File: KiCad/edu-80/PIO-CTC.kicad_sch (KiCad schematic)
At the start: 2 parts, among them U2 Z84C20, U3 Z8430_CTC

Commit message: Working on removing edu-80-rescue symbol library
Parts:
- U3: symbol edu-80-rescue:Z8430_CTC-Edu-80_Symbol -> Edu-80_Symbols:Z8430_CTC
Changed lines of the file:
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@@
     )
   )
-  (symbol (lib_id "edu-80-rescue:Z8430_CTC-Edu-80_Symbol") (at 161.29 129.54 0) (unit 1)
+  (symbol (lib_id "Edu-80_Symbols:Z8430_CTC") (at 161.29 129.54 0) (unit 1)
     (in_bom yes) (on_board yes) (dnp no)
     (property "Reference" "U3" (at 168.91 110.49 0)

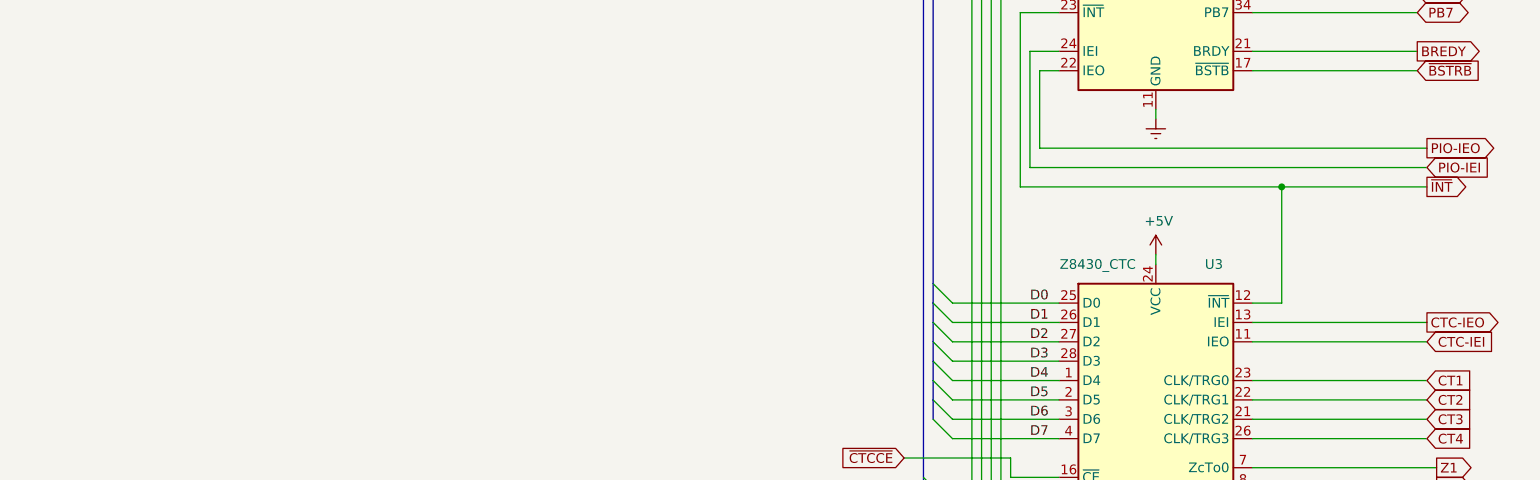
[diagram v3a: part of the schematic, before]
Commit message: Fixed ~IRQ vs. INT for PIO/CTC. Removed old (version 5) schematic files.
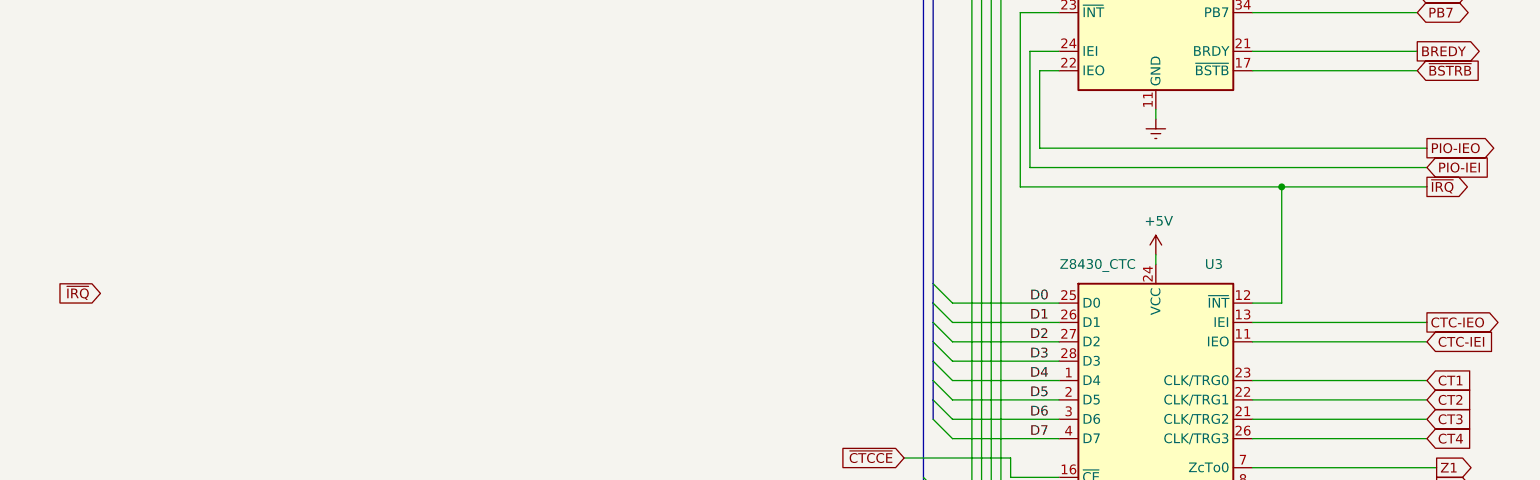
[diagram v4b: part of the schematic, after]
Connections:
- net ~{INT} renamed ~{IRQ}
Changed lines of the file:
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@@
   (title_block
     (title "Edu-80 Z80 Trainer")
-    (date "2023-06-03")
+    (date "2023-06-05")
     (rev "0.1")
     (company "Strangers")
-    (comment 1 "Author: James D. Tucker")
+    (comment 4 "Author: James D. Tucker")
   )
   (junction (at 139.7 67.31) (diameter 0) (color 0 0 0 0)
@@
     )
   )
+  (global_label "~{IRQ}" (shape output) (at 196.85 100.33 0)
+    (effects (font (size 1.27 1.27)) (justify left))
+    (property "Intersheetrefs" "${INTERSHEET_REFS}" (at 196.85 100.33 0)
+      (effects (font (size 1.27 1.27)) hide)
+    )
+  )
   (global_label "PB7" (shape tri_state) (at 195.58 77.47 0)
     (effects (font (size 1.27 1.27)) (justify left))
@@
     )
   )
+  (global_label "~{IRQ}" (shape input) (at 22.86 114.3 180)
+    (effects (font (size 1.27 1.27)) (justify right))
+    (property "Intersheetrefs" "${INTERSHEET_REFS}" (at 22.86 114.3 0)
+      (effects (font (size 1.27 1.27)) hide)
+    )
+  )
   (global_label "CT1" (shape input) (at 196.85 125.73 0)
     (effects (font (size 1.27 1.27)) (justify left))
@@
       (effects (font (size 1.27 1.27)) hide)
     )
-  )
-  (global_label "~{INT}" (shape output) (at 196.85 100.33 0)
-    (effects (font (size 1.27 1.27)) (justify left))
-    (property "Intersheetrefs" "${INTERSHEET_REFS}" (at 196.85 100.33 0)
-      (effects (font (size 1.27 1.27)) hide)
-    )
